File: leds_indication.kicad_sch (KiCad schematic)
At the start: 8 parts, among them U8 74HC595

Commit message: progress
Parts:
- D9: footprint ftdi_quad_lin:1296.3004 -> ftdi_quad_lin:1276.2004
- R17, R19, R20: value 330R -> 1k
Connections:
- net +5V: now also D9.1, D9.3, D9.5, D9.7
- net GND: no longer D9.1, D9.3, D9.5, D9.7
- net led_indication_2/INDICATION: now reaches U8.5 (QF)
- net led_indication_2/INDICATION: no longer R20.2
- net led_indication_1/INDICATION: now reaches U8.3 (QD)
- net led_indication_1/INDICATION: no longer R19.2
- net led_indication_3/INDICATION: now reaches U8.7 (QH)
- net led_indication_3/INDICATION: no longer R21.2
- net led_indication_0/INDICATION: now reaches U8.1 (QB)
- net led_indication_0/INDICATION: no longer R17.2
- new net led_indication_0/LED: R17.2
- new net led_indication_1/LED: R19.2
- new net led_indication_2/LED: R20.2
- new net led_indication_3/LED: R21.2
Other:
- added sheet led_indication_0 (led_indication.kicad_sch)
- added sheet led_indication_1 (led_indication.kicad_sch)
- added sheet led_indication_2 (led_indication.kicad_sch)
- added sheet led_indication_3 (led_indication.kicad_sch)
- note added: "RX channels"
- moved on the sheet: C26, D9A, D9B, D9C, D9D, R17, R18, R19, R20, R21, U8

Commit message: progress
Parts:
- added D14, D15, D16, D17: LED, ftdi_quad_lin:1216.1002, symbol Device:LED
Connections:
- net +5V: now also D14.2 (A), D15.2 (A), D16.2 (A), D17.2 (A); no longer D9.1, D9.3, D9.5, D9.7
- net at R20.1: now also D16.1 (K); no longer D9.6
- net at R19.1: now also D15.1 (K); no longer D9.4
- net at R21.1: now also D17.1 (K); no longer D9.8
- net at D9.2: no longer R17.1
- new net: D14.1 (K), R17.1

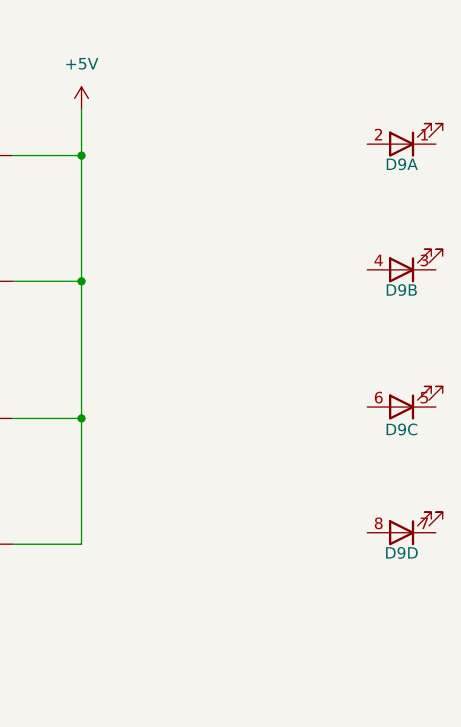
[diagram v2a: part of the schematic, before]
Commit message: new connectors
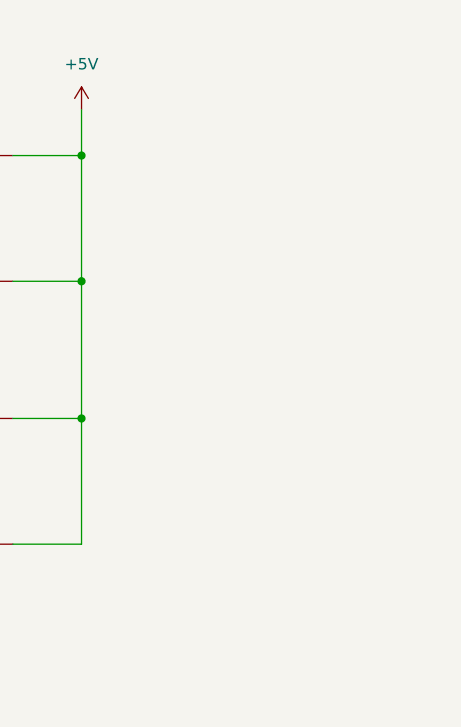
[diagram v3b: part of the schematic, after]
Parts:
- removed D9: ~, ftdi_quad_lin:1276.2004, symbol ftdi_quad_lin:led_array_4

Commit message: reworking
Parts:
- added J7: Conn_01x05, Connector_JST:JST_XH_B5B-XH-A_1x05_P2.50mm_Vertical, symbol Connector_Generic:Conn_01x05
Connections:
- net +5V: now also J7.5 (Pin_5)
- net at D16.1 (K), R20.1: now also J7.3 (Pin_3)
- net at D17.1 (K), R21.1: now also J7.4 (Pin_4)
- net at D15.1 (K), R19.1: now also J7.2 (Pin_2)
- net at D14.1 (K), R17.1: now also J7.1 (Pin_1)
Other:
- moved on the sheet: D14, D15, D16, D17

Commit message: yep crash
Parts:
- R21: value 330R -> 1k
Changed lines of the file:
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@@
 			)
 		)
-		(property "Value" "330R"
+		(property "Value" "1k"
 			(at 219.71 114.554 90)
 			(effects

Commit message: Added manfs
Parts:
- J7: manf# (none) -> B5B-XH-A (LF)(SN)
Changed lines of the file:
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@@
+			)
+		)
+		(property "manf#" "B5B-XH-A (LF)(SN)"
+			(at 222.25 58.42 0)
+			(effects
+				(font
+					(size 1.27 1.27)
+				)
+				(hide yes)
 			)
 		)

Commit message: more capacitors
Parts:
- added C38, C39: 100nF, Capacitor_SMD:C_0805_2012Metric, symbol Device:C
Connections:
- net +5V: now also C38.1, C39.1
- net GND: now also C38.2, C39.2

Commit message: more capacitors
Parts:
- added C40, C41, C42, C43: 100nF, Capacitor_SMD:C_0805_2012Metric, symbol Device:C
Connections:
- net +5V: now also C40.1, C41.1, C42.1, C43.1
- net GND: now also C40.2, C41.2, C42.2, C43.2
